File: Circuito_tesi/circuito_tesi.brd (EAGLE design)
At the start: 30 parts, among them IC1 317T, IC2 317T, U1 NRF52832, U2 BME688, U3 MICS-6814

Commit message: modifica board
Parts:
- removed IC1, IC2: 317T, linear:TO220H
- added 300_OHM: 1614992-1, 1614992-1:RESAD640W45L370D200
- added IC3.3, IC5: 317T, linear:TO220H
- added LED1: LAP4-BOTTOM, led:P47F-BOTTOM
- added S1: GF-123-0054, GF-123-0054:SW_GF-123-0054
- added U4, U5: OPA2277PA, OPA2277PA:DIP794W45P254L959H508Q8
- moved C7 430.2 mm to (94.0, 45.7)
- moved C4 419.1 mm to (82.5, 48.3)
- moved C3 408.3 mm to (73.7, 48.3)
- moved 10_MOHM2 373.4 mm to (-19.1, 94.0)
- moved 5_MOHM2 357.9 mm to (-39.4, 94.0)
- moved 820OHM 357.7 mm to (86.0, 63.6), turned to 90 degrees
- moved 27OHM 355.4 mm to (91.4, 63.5), turned to 90 degrees
- moved 5_MOHM1 353.5 mm to (-29.2, 94.0)
- moved 130OHM 353.3 mm to (95.2, 64.8), turned to 90 degrees
- moved 10_MOHM 327.3 mm to (-49.5, 94.0)
- moved 5_MOHM 321.7 mm to (-59.7, 94.0)
- moved BT4 311.3 mm to (62.2, 66.0)
- moved 10_MOHM1 309.0 mm to (-100.3, 73.7)
- moved BT3 261.8 mm to (21.6, 66.0)
- moved U3 241.0 mm to (92.7, 53.3), turned to 270 degrees
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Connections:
- removed net N$15: 5_MOHM.2
- new net N$19: BT1.1, BT1.1_1, S1.1
- new net N$21: LED1.A, U1.28
- new net N$22: 5_MOHM.2, U4.1, U4.2
- new net VDD: C1.1, C5.1, IC3.3.3, IC5.3, S1.2
- net 3.3: now also IC3.3.2; no longer C1.2, C2.2, C5.2, C6.2, IC1.1, IC2.1, IC2.2
- net 5V: now also IC5.2, U4.8, U5.8; no longer IC1.2
- net GND: now also 300_OHM.1, C1.2, C2.2, C5.2, C6.2, IC3.3.1, IC5.1, U4.4, U5.4
- net N$10: now also U4.3
- net N$14: now also U5.3
- net N$6: now also U4.5
- net N$7: now also U4.6, U4.7
- net N$8: now also U5.1, U5.2
- net N$9: now also 300_OHM.2, LED1.C; no longer BT1.1, BT1.1_1, C1.1, C5.1, IC1.3, IC2.3
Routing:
- net VDD: track 0.00 -> 191.7 mm
- net N$4: track 0.00 -> 95.9 mm
- net N$19: track 0.00 -> 90.0 mm
- net SCL: track 0.00 -> 80.3 mm
- net SDA: track 0.00 -> 79.3 mm
- net 5V: track 0.00 -> 70.3 mm
- net N$5: track 0.00 -> 67.6 mm
- net N$2: track 0.00 -> 64.8 mm
- net 3.3: track 0.00 -> 43.4 mm
- net GND: track 0.00 -> 25.5 mm
- net N$21: track 0.00 -> 11.5 mm
- net N$9: track 0.00 -> 11.4 mm
- net N$11: track 0.00 -> 9.80 mm
- net N$13: track 0.00 -> 7.25 mm
- net N$3: track 0.00 -> 6.66 mm
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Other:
- board outline added: 100 x 80 mm

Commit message: Aggiunti circuiti su board
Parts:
- moved U4 162.0 mm to (40.6, 63.5)
- moved U5 153.7 mm to (27.9, 44.5), turned to 180 degrees
- moved 10_MOHM1 142.7 mm to (39.4, 44.5), turned to 90 degrees
- moved 5_MOHM 114.6 mm to (50.8, 63.5), turned to 90 degrees
- moved 10_MOHM 107.8 mm to (50.8, 54.6), turned to 90 degrees
- moved 5_MOHM2 95.0 mm to (35.6, 35.6), turned to 90 degrees
- moved C5 83.9 mm to (16.5, 49.5)
- moved C1 82.7 mm to (15.2, 8.89)
- moved 10_MOHM2 82.6 mm to (39.4, 35.6), turned to 270 degrees
- moved C2 81.4 mm to (11.4, 8.89)
- moved C6 81.1 mm to (11.4, 47.0)
- moved IC5 80.8 mm to (12.7, 62.2)
- moved IC3.3 80.5 mm to (12.7, 22.9)
- moved 5_MOHM1 80.0 mm to (39.4, 52.7), turned to 90 degrees
- moved 130OHM 74.9 mm to (20.3, 63.5), turned to 270 degrees
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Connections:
- net 3.3: no longer B1.GND1, B1.GND2
- net GND: now also B1.GND1, B1.GND2
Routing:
- net VDD: track 191.7 -> 66.2 mm
- net N$4: track 95.9 -> 37.7 mm
- net 5V: track 70.3 -> 120.3 mm
- net 3.3: track 43.4 -> 93.1 mm
- net N$16: track 0.00 -> 39.7 mm, vias 0 -> 2
- net SDA: track 79.3 -> 44.4 mm, vias 0 -> 2
- net SCL: track 80.3 -> 45.8 mm
- net N$18: track 0.00 -> 29.9 mm, vias 0 -> 2
- net N$14: track 0.00 -> 27.0 mm
- net GND: track 25.5 -> 0.00 mm
- net N$6: track 0.00 -> 21.9 mm
- net N$17: track 0.00 -> 19.9 mm
- net N$22: track 0.00 -> 17.5 mm
- net N$19: track 90.0 -> 104.0 mm
- net N$7: track 0.00 -> 14.0 mm
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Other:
- outline, holes or cut-outs redrawn

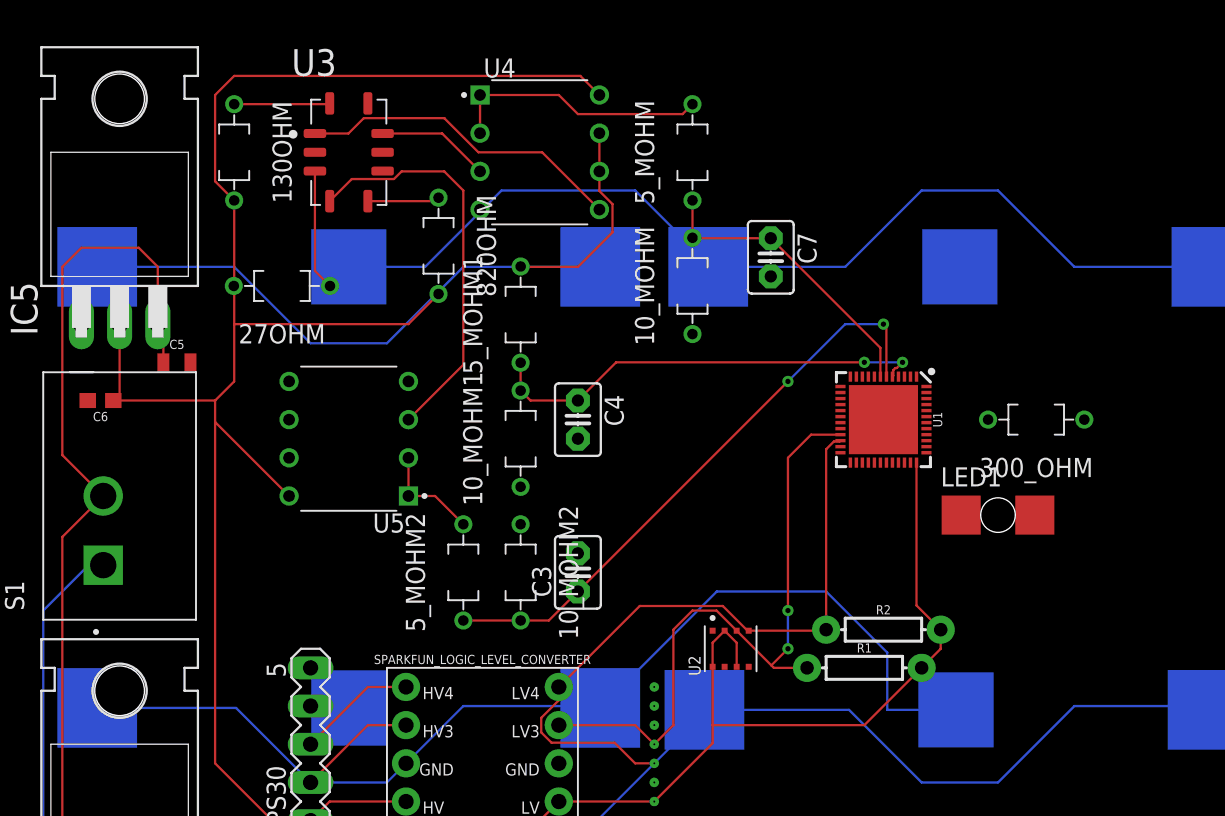
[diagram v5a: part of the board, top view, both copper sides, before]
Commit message: Aggiunte resistenze e condensatori smd
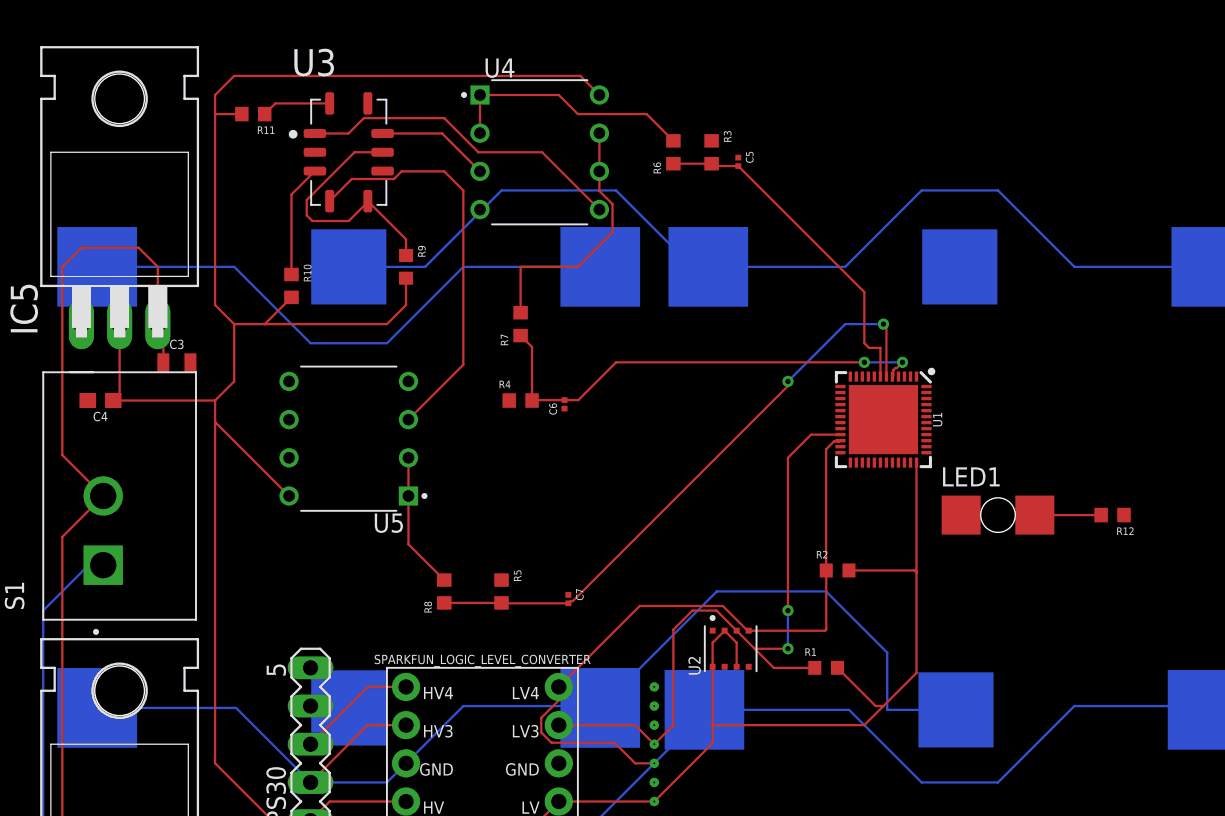
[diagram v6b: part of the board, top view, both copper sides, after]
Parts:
- removed 10_MOHM, 10_MOHM1, 10_MOHM2, 130OHM, 27OHM, 300_OHM, 5_MOHM, 5_MOHM1, 5_MOHM2, 820OHM: 1614992-1, 1614992-1:RESAD640W45L370D200
- added R10: RMCF0603FT270R, Res_270OHM:RESC1508X55N
- added R11: RMCF0603FT130R, Res_130OHM:RESC1508X55N
- added R12: RMCF0603FT300R, Res_300OHM:RESC1508X55N
- added R3, R4, R5: RMCF0603FT10M0, Res_10MOHM_2:RESC1508X55N
- added R6, R7, R8: RMCF0603FT5M10, Res_5.1MOHM:RESC1508X55N
- added R9: RNCF0603DTE820R, Res_820OHM:RESC1508X55N
- C3: value (none) -> 0.33µF; device capacitor-wima:C2.5-3 -> SparkFun-Capacitors:0805
- C4: value (none) -> 0.1uF; device capacitor-wima:C2.5-3 -> SparkFun-Capacitors:0603
- C5: value 0.33µF -> GRM033R60J103KA01D; device SparkFun-Capacitors:0805 -> Condens_10nF:CAPC0603X33N
- C6: value 0.1uF -> GRM033R60J103KA01D; device SparkFun-Capacitors:0603 -> Condens_10nF:CAPC0603X33N
- C7: value (none) -> GRM033R60J103KA01D; device capacitor-wima:C2.5-3 -> Condens_10nF:CAPC0603X33N
- R1, R2: value 10k -> RNCF0603BTE10K0; device SparkFun-Resistors:AXIAL-0.3 -> Res_10KOHM:RESC1508X55N
- moved C5 39.6 mm to (53.8, 62.9), turned to 270 degrees
- moved C4 31.8 mm to (11.4, 47.0), turned to 180 degrees
- moved C6 30.9 mm to (42.3, 46.7), turned to 90 degrees
- moved C3 30.1 mm to (16.5, 49.5), turned to 0 degrees
- moved C7 26.4 mm to (42.5, 33.8)
- moved R2 4.98 mm to (60.5, 35.7)
- moved R1 2.54 mm to (59.7, 29.2)
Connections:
- removed net N$18: 10_MOHM1.2, 5_MOHM1.1, C4.1, U1.5
- new net N$15: C6.2, R4.2, R7.1, U1.5
- net 3.3: now also R1.2, R2.2; no longer R1.P$2, R2.P$2
- net 5V: now also C4.1, R10.2, R11.2, R9.2; no longer 130OHM.2, 27OHM.2, 820OHM.2, C6.1
- net GND: now also C5.1, C6.1, C7.1, R12.1, R3.1, R4.1, R5.1; no longer 10_MOHM.1, 10_MOHM1.1, 10_MOHM2.1, 300_OHM.1, C5.2, C6.2, C7.2
- net N$11: now also R9.1; no longer 820OHM.1
- net N$12: now also R10.1; no longer 27OHM.1
- net N$13: now also R11.1; no longer 130OHM.1
- net N$16: now also C7.2, R5.2, R8.1; no longer 10_MOHM2.2, 5_MOHM2.1, C3.1
- net N$17: now also C5.2, R3.2, R6.1; no longer 10_MOHM.2, 5_MOHM.1, C7.1
- net N$22: now also R6.2; no longer 5_MOHM.2
- net N$7: now also R7.2; no longer 5_MOHM1.2
- net N$8: now also R8.2; no longer 5_MOHM2.2
- net N$9: now also R12.2; no longer 300_OHM.2
- net SCL: now also R2.1; no longer R2.P$1
- net SDA: now also R1.1; no longer R1.P$1
- net VDD: now also C3.1; no longer C5.1
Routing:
- net N$15: track 0.00 -> 31.6 mm, vias 0 -> 2
- net N$18: track 29.9 -> 0.00 mm, vias 2 -> 0
- net N$11: track 4.79 -> 16.8 mm
- net 3.3: track 93.1 -> 100.4 mm
- net N$9: track 0.00 -> 4.41 mm
- net 5V: track 120.3 -> 123.9 mm
- net N$7: track 14.0 -> 17.1 mm
- net N$17: track 19.9 -> 22.7 mm
- net N$8: track 6.97 -> 9.12 mm
- net N$13: track 6.37 -> 4.68 mm
- net SDA: track 44.4 -> 45.6 mm
- net N$16: track 39.7 -> 40.7 mm
- net N$22: track 17.5 -> 16.7 mm
- net N$12: track 8.06 -> 7.53 mm

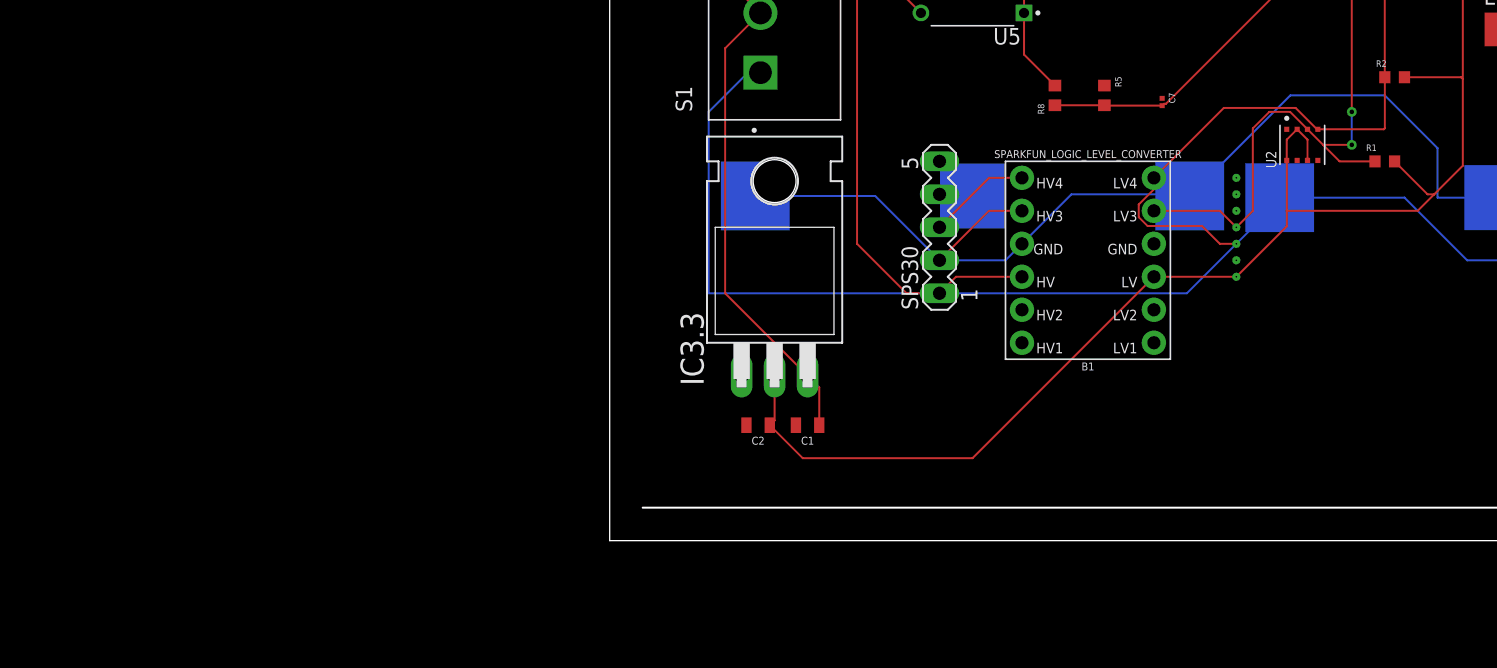
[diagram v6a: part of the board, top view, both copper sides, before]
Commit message: Aggiunto BME280 e SGP30
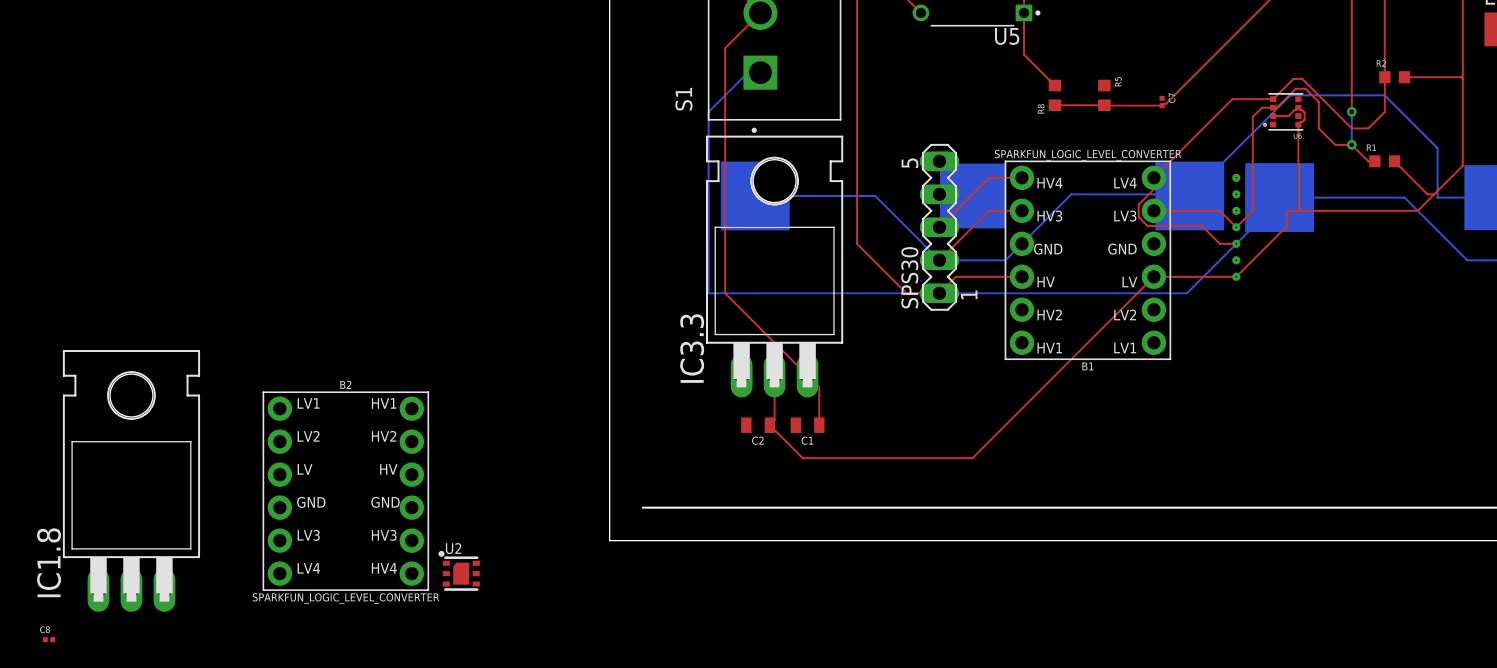
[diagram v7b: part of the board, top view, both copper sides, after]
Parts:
- added B2: SPARKFUN_LOGIC_LEVEL_CONVERTER, SparkFun-Boards:SPARKFUN_LOGIC_LEVEL_CONVERTER
- added C8: GRM033C80J104KE15D, Condens_100nF:CAPC0603X33N
- added IC1.8: 317T, linear:TO220H
- added U6: BME280, BME280:PSON65P250X250X100-8N
- U2: value BME688 -> SGP30; device BME688:IC_BME688 -> SGP30:SGP30
- moved U2 72.7 mm to (-11.4, -2.54), turned to 0 degrees
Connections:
- removed net VDDH: SCD4X.19
- new net 1.8V: B2.LV, C8.1, IC1.8.2, U2.1, U2.5
- new net N$20: B2.LV3, U2.3
- new net N$23: B2.LV4, U2.6
- net 3.3: now also B2.HV, SCD4X.19, U6.2, U6.6, U6.8; no longer U2.2, U2.6, U2.8
- net GND: now also B2.GND1, B2.GND2, C8.2, IC1.8.1, U2.2, U2.4, U2.DIEPAD, U6.1, U6.5, U6.7; no longer U2.1, U2.5, U2.7
- net SCL: now also B2.HV4, U6.4; no longer U2.4
- net SDA: now also B2.HV3, U6.3; no longer U2.3
- net VDD: now also IC1.8.3
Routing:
- net 3.3: track 100.4 -> 101.9 mm
- net SCL: track 45.9 -> 47.0 mm
- net SDA: track 45.6 -> 46.5 mm

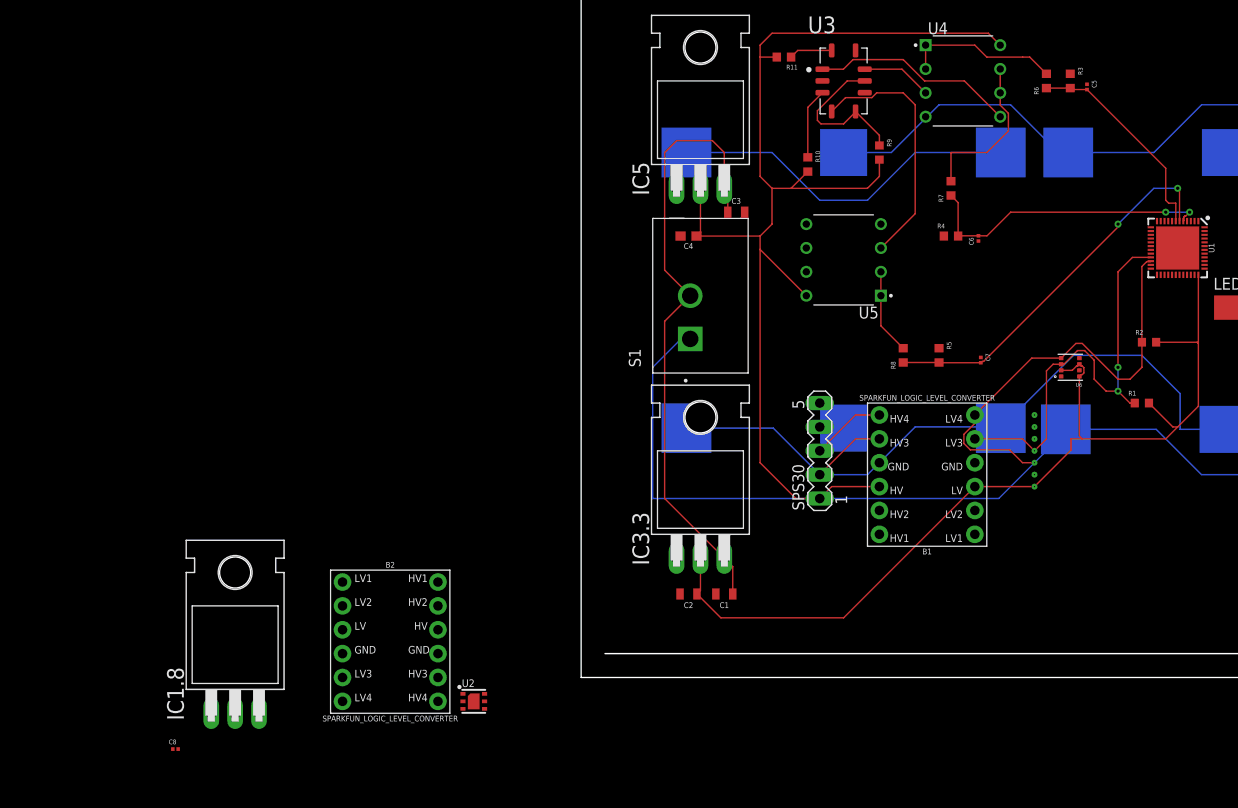
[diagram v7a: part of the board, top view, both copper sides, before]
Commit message: Aggiunto ACCELEROMETRO
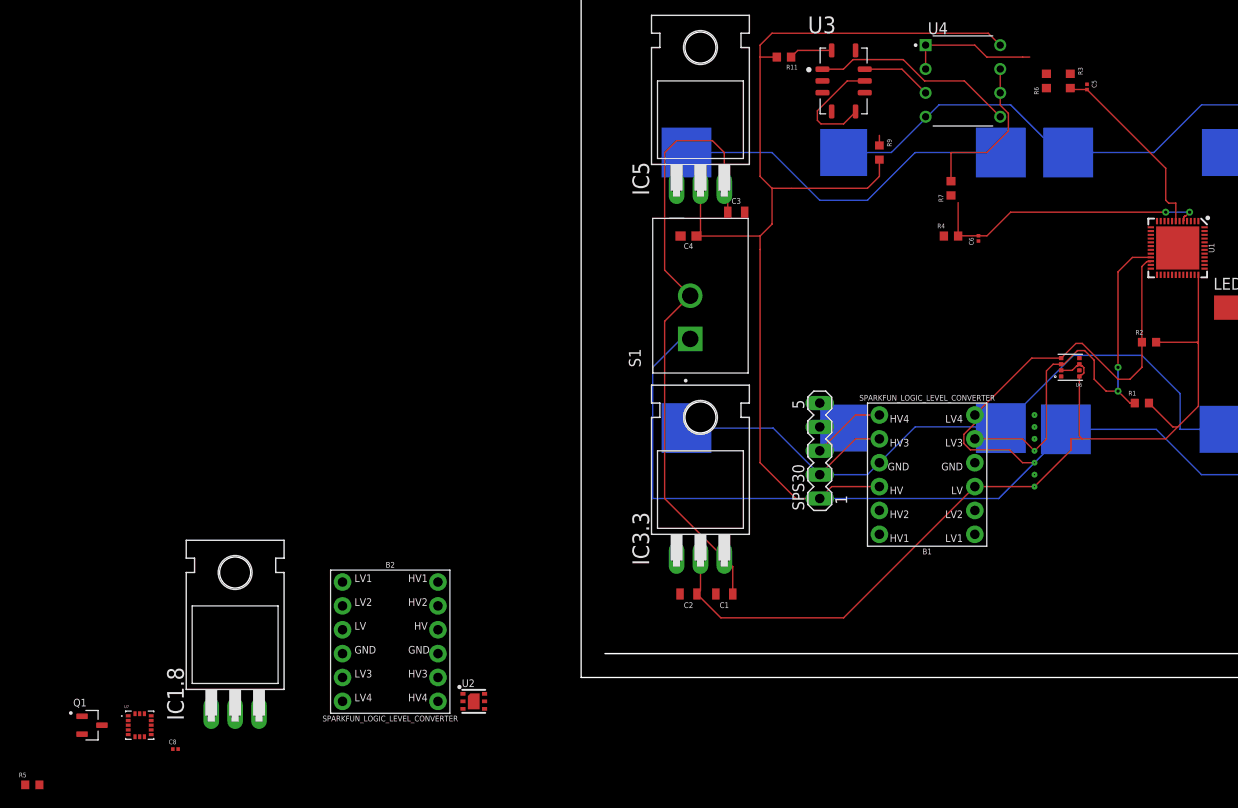
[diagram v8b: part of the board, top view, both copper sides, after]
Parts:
- removed C7: GRM033R60J103KA01D, Condens_10nF:CAPC0603X33N
- removed R10: RMCF0603FT270R, Res_270OHM:RESC1508X55N
- removed R8: RMCF0603FT5M10, Res_5.1MOHM:RESC1508X55N
- removed U5: OPA2277PA, OPA2277PA:DIP794W45P254L959H508Q8
- added Q1: BSS138, BSS138:SOT95P240X111-3N
- added U7: LIS3DH, LIS3DH:PQFN50P300X300X100-16N
- R5: value RMCF0603FT10M0 -> RNCF0603BTE10K0; device Res_10MOHM_2:RESC1508X55N -> Res_10KOHM:RESC1508X55N
- moved R5 106.8 mm to (-58.4, -11.4), turned to 0 degrees
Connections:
- removed net N$12: R10.1, U3.C
- removed net N$14: U3.D, U5.3
- removed net N$16: C7.2, R5.2, R8.1, U1.6
- net 1.8V: now also U7.1, U7.14, U7.8
- net 5V: no longer R10.2, U5.8
- net GND: now also U7.10, U7.12, U7.5, U7.7; no longer C7.1, R5.1, U3.F, U5.4
- net N$11: no longer U3.E
- net N$17: now also R6.2; no longer R6.1
- net N$20: now also U7.6
- net N$22: now also R6.1; no longer R6.2
- net N$23: now also U7.4
- net N$8: now also R5.2; no longer R8.2, U5.1, U5.2
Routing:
- net N$16: track 40.7 -> 0.00 mm, vias 2 -> 0
- net N$14: track 27.0 -> 0.00 mm
- net 5V: track 123.9 -> 114.5 mm
- net N$8: track 9.12 -> 0.00 mm
- net N$12: track 7.53 -> 0.00 mm
- net N$11: track 16.8 -> 13.2 mm
- net N$17: track 22.7 -> 20.2 mm
- net N$22: track 16.7 -> 14.1 mm
- net N$15: track 31.6 -> 30.5 mm
